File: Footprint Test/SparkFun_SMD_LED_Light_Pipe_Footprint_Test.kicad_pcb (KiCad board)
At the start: 2 copper layers, 21.3 x 33 mm, 21 parts, among them J1 Conn_01x04

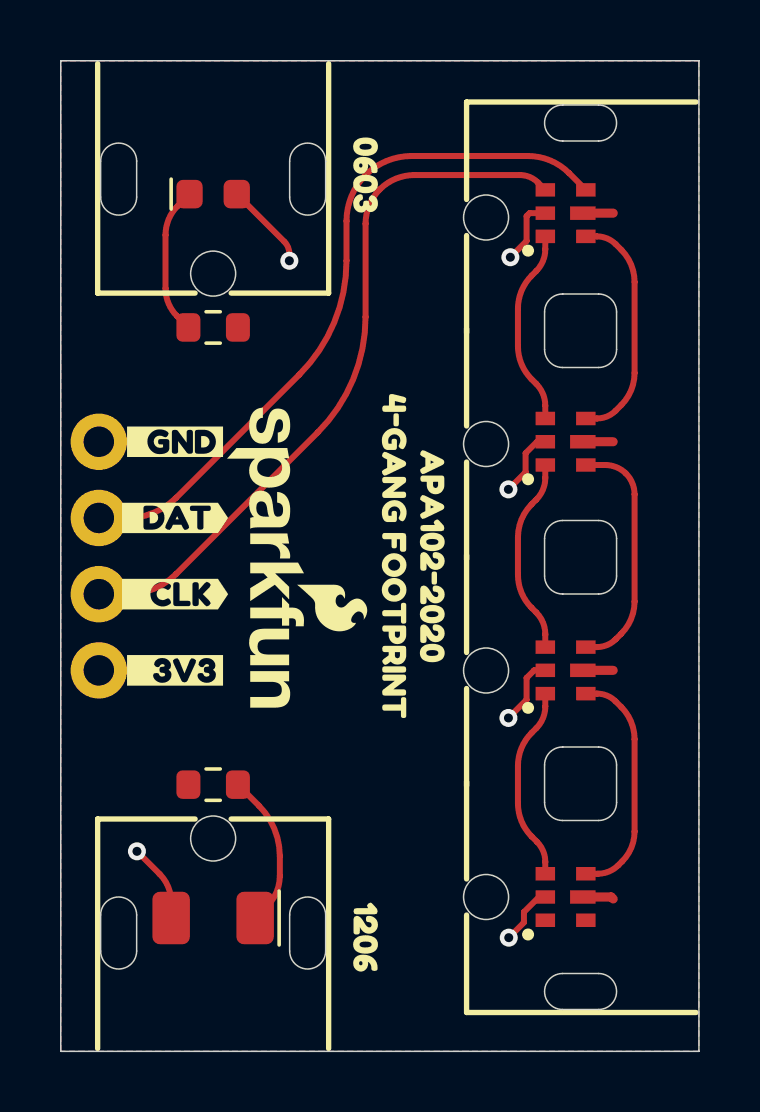
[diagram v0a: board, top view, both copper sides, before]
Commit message: Update layout with 3D model
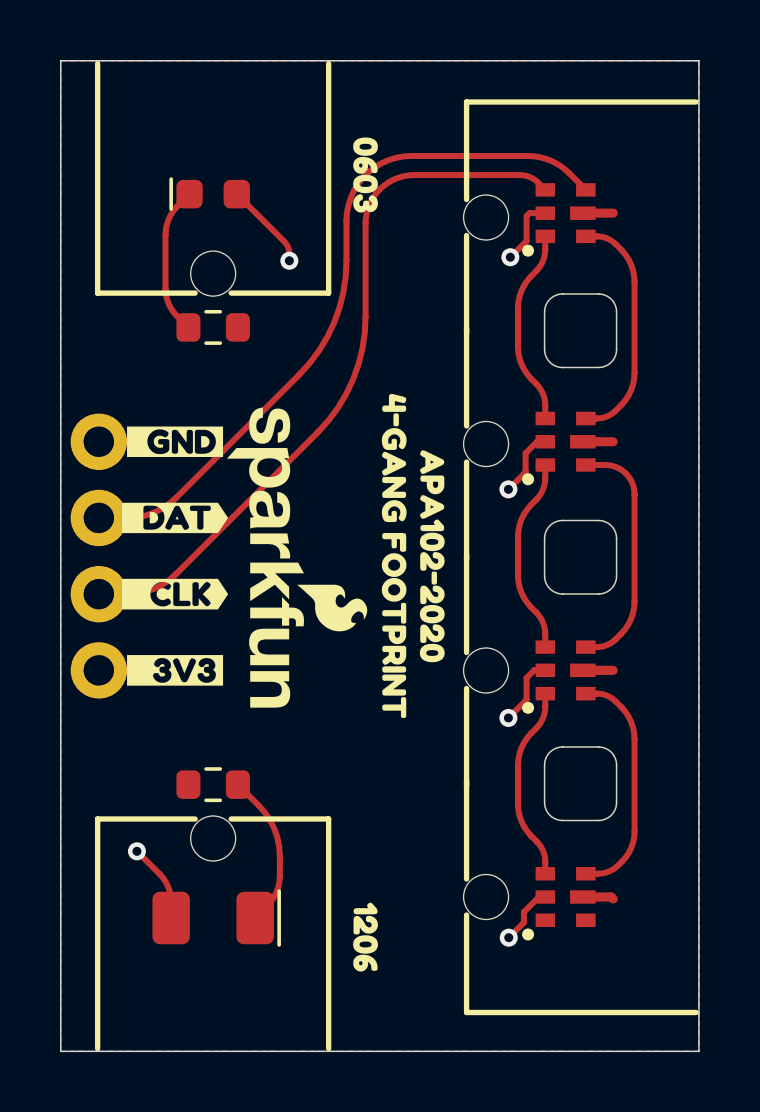
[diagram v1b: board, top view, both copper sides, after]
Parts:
- D2: footprint SparkFun SMD LED Light Pipe:LED_0603_1608Metric -> SparkFun-LED:LED_0603_1608Metric_Blue
- D4: footprint SparkFun SMD LED Light Pipe:LED_1206_3216Metric -> SparkFun-LED:LED_1206_3216Metric
- J1: footprint SparkFun SMD LED Light Pipe:1x04 -> SparkFun-Connector:1x04
- R1, R2: footprint SparkFun SMD LED Light Pipe:R_0603_1608Metric -> SparkFun-Resistor:R_0603_1608Metric
